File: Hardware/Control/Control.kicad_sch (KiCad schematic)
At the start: 44 parts, among them SW1 EN11-HSM1AF20, SW2 KO128B2007, SW3 Conn_01x04, U1 XRA1402IG16TR-F, U2 FT230XS-U, U4 ATMEGA328P-AU, U5 ESDALD05UD4, Y1 ABM8AIG-20.000MHZ-4-T

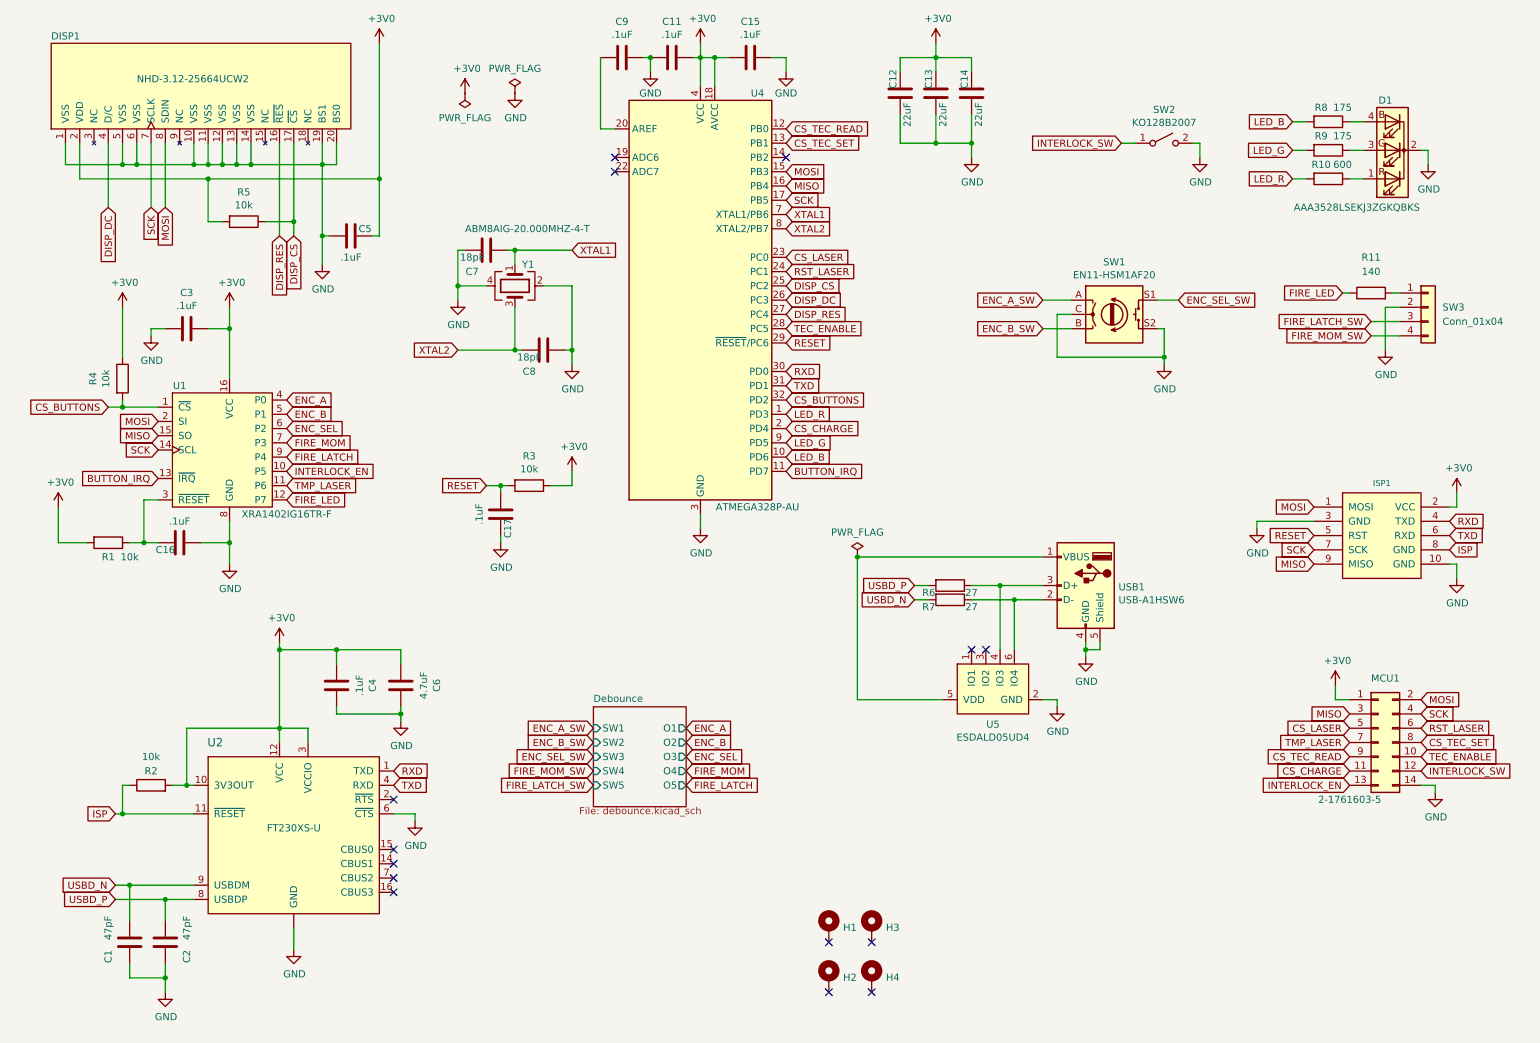
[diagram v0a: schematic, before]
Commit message: Move to AVR128DB64 MCU
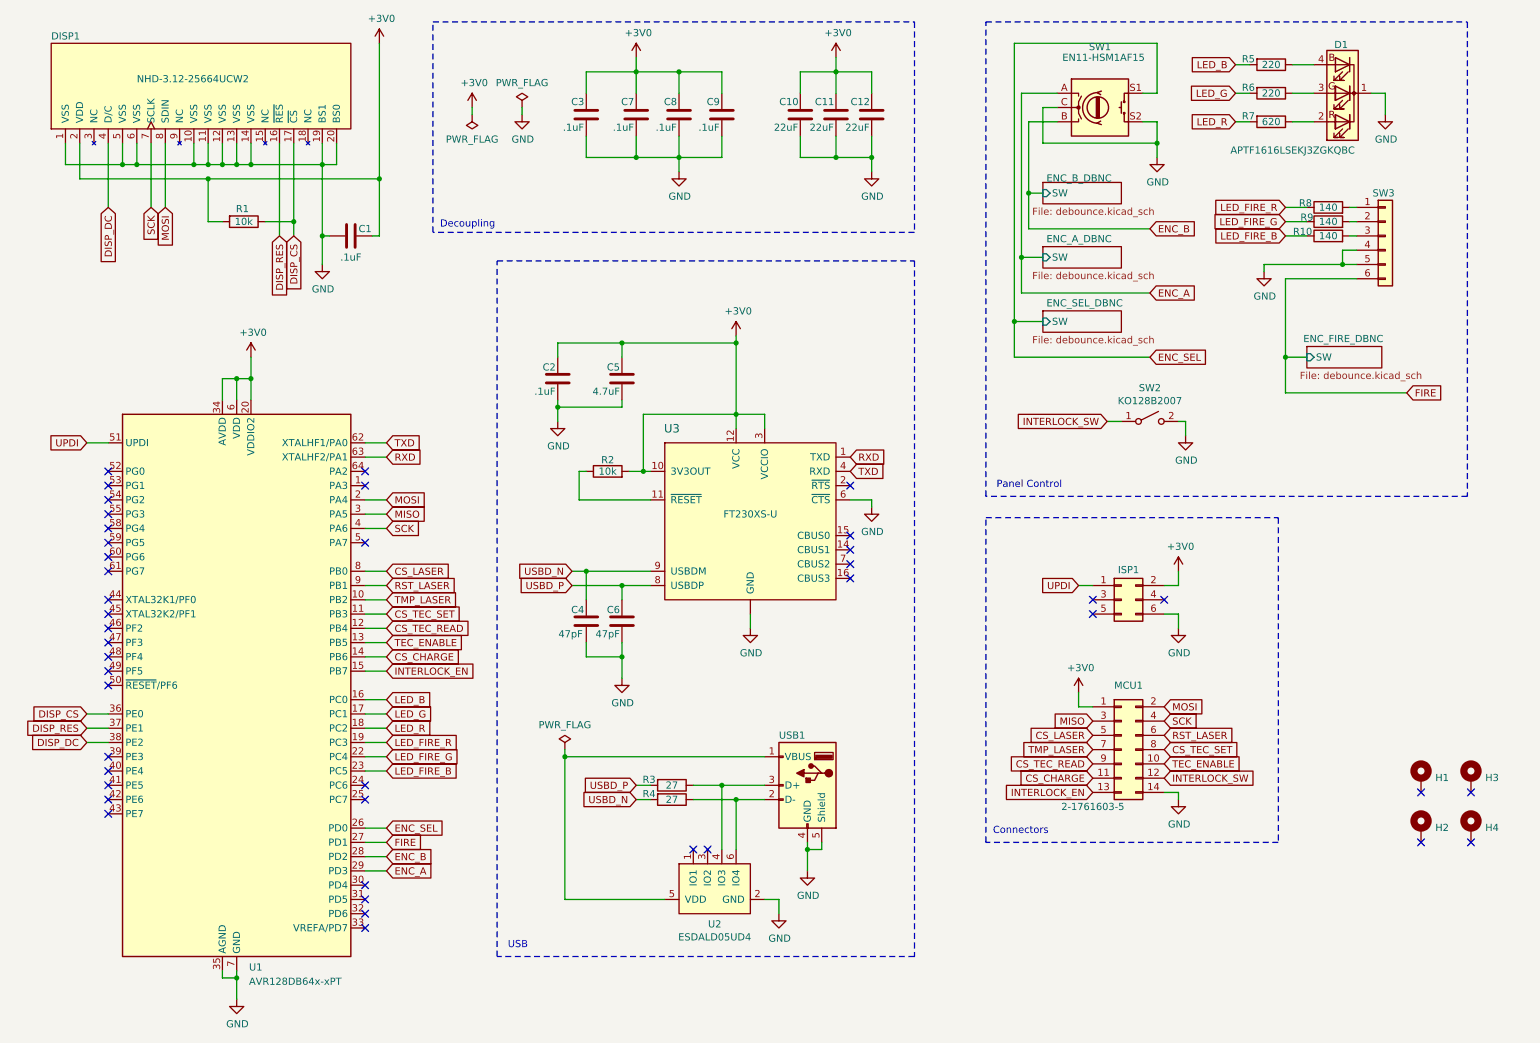
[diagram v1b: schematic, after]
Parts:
- removed C11, C15, C16, C17: .1uF, Capacitor_SMD:C_0805_2012Metric, symbol Device:C
- removed D1: AAA3528LSEKJ3ZGKQBKS, LED_SMD:LED_Avago_PLCC4_3.2x2.8mm_CW, symbol Device:LED_RKGB
- removed ISP1: AVR_ISP_10_SERIAL, pepin-footprints:TC2050-IDC, symbol pepin_con:AVR_ISP_10_SERIAL
- removed R1, R3, R4: 10k, Resistor_SMD:R_0805_2012Metric, symbol Device:R
- removed SW3: Conn_01x04, Connector_PinHeader_2.54mm:PinHeader_1x04_P2.54mm_Vertical, symbol Connector_Generic:Conn_01x04
- removed U1: XRA1402IG16TR-F, Package_SO:TSSOP-16_4.4x5mm_P0.65mm, symbol Components:XRA1402IG16TR-F
- removed U4: ATMEGA328P-AU, Package_QFP:TQFP-32_7x7mm_P0.8mm, symbol MCU_Microchip_ATmega:ATmega328P-A
- removed Y1: ABM8AIG-20.000MHZ-4-T, Crystal:Crystal_SMD_3225-4Pin_3.2x2.5mm, symbol Device:Crystal_GND24
- added D1: APTF1616LSEKJ3ZGKQBC, Components:LED_Kingbright_KRGB_1.6x1.6mm, symbol Device:LED_KRGB
- added ISP1: 61200621621, Connector_IDC:IDC-Header_2x03_P2.54mm_Vertical, symbol Connector_Generic:Conn_02x03_Odd_Even
- added R10, R9: 140, Resistor_SMD:R_0805_2012Metric, symbol Device:R
- added SW3: Conn_01x06, Connector_PinHeader_2.54mm:PinHeader_1x06_P2.54mm_Vertical, symbol Connector_Generic:Conn_01x06
- added U1: AVR128DB64x-xPT, Package_QFP:TQFP-64_10x10mm_P0.5mm, symbol MCU_Microchip_AVR_Dx:AVR128DB64x-xPT
- C1: renamed from C5; Product Number (none) -> CGA4J2X8R1H104K125AE
- C10: renamed from C12; Product Number CL31A226KAHNNNE -> LMJ316BB7226KLHT
- C11: renamed from C13; Product Number CL31A226KAHNNNE -> LMJ316BB7226KLHT
- C12: renamed from C14; Product Number CL31A226KAHNNNE -> LMJ316BB7226KLHT
- C2: renamed from C4; Product Number (none) -> CGA4J2X8R1H104K125AE
- C3, C9: Product Number (none) -> CGA4J2X8R1H104K125AE
- C4: renamed from C1; Product Number (none) -> C0805C470J1GAC
- C5: renamed from C6; Product Number (none) -> C0805C475K4RACAUTO
- C6: renamed from C2; Product Number (none) -> C0805C470J1GAC
- C7, C8: value 18pF -> .1uF; Product Number C0805C180J5HACTU -> CGA4J2X8R1H104K125AE
- R1: renamed from R5; Product Number (none) -> ERA-6AEB103V
- R2: Product Number (none) -> ERA-6AEB103V
- R3: renamed from R6; Product Number (none) -> CR0805-FX-27R0ELF
- R4: renamed from R7; Product Number (none) -> CR0805-FX-27R0ELF
- R5: renamed from R8; value 175 -> 220; Product Number (none) -> ERA-6AEB221V
- R6: renamed from R9; value 175 -> 220; Product Number (none) -> ERA-6AEB221V
- R7: renamed from R10; value 600 -> 620; Product Number (none) -> CR0805-FX-6200ELF
- R8: renamed from R11; Product Number (none) -> CRCW0805140RFKEA
- SW1: value EN11-HSM1AF20 -> EN11-HSM1AF15; Product Number EN11-HSM1AF20 -> EN11-HSM1AF15
- USB1: value USB-A1HSW6 -> UJ2-A-HR-G-TH; Product Number USB-A1HSW6 -> UJ2-A-HR-G-TH
- renumbered U5 to U2, U2 to U3
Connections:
- net ENC_A_SW is gone; now on net ENC_A: SW1.A
- net ENC_B_SW is gone; now on net ENC_B: SW1.B
- net ENC_SEL_SW is gone; now on net ENC_SEL: SW1.S1
- net XTAL1 is gone; now on net GND: C7.1
- net XTAL2 is gone; now on net +3V0: C8.2
- net +3V0: now also C7.2, C9.2, ISP1.2 (Pin_2), U1.20 (VDDIO2), U1.34 (AVDD), U1.56 (VDD), U1.6 (VDD)
- net CS_CHARGE: now also U1.14 (PB6)
- net CS_LASER: now also U1.8 (PB0)
- net CS_TEC_READ: now also U1.12 (PB4)
- net CS_TEC_SET: now also U1.11 (PB3)
- net DISP_CS: now also U1.36 (PE0)
- net DISP_DC: now also U1.38 (PE2)
- net DISP_RES: now also U1.37 (PE1)
- net ENC_A: now also U1.29 (PD3)
- net ENC_B: now also U1.28 (PD2)
- net ENC_SEL: now also U1.26 (PD0)
- net GND: now also C9.1, D1.1 (K), ISP1.6 (Pin_6), SW3.4 (Pin_4), SW3.5 (Pin_5), U1.21 (GND), U1.35 (AGND), U1.57 (GND), U1.7 (GND); no longer C7.2, C9.2
- net INTERLOCK_EN: now also U1.15 (PB7)
- net LED_B: now also U1.16 (PC0)
- net LED_G: now also U1.17 (PC1)
- net LED_R: now also U1.18 (PC2)
- net MISO: now also U1.3 (PA5)
- net MOSI: now also U1.2 (PA4)
- net RST_LASER: now also U1.9 (PB1)
- net RXD: now also U1.63 (XTALHF2/PA1)
- net SCK: now also U1.4 (PA6)
- net TEC_ENABLE: now also U1.13 (PB5)
- net TMP_LASER: now also U1.10 (PB2)
- net TXD: now also U1.62 (XTALHF1/PA0)
- net at R5.1: now also D1.4 (BA)
- net at R6.1: now also D1.3 (GA)
- net at R7.1: now also D1.2 (RA)
- net at R8.2: now also SW3.1 (Pin_1)
- net FIRE_LED renamed LED_FIRE_R
- net LED_FIRE_R: now also U1.19 (PC3)
- net ISP: no longer names the net of R2.1, U3.11 (~{RESET})
- new net: R9.2, SW3.2 (Pin_2)
- new net: R10.2, SW3.3 (Pin_3)
- new net FIRE: SW3.6 (Pin_6), U1.27 (PD1)
- new net LED_FIRE_B: R10.1, U1.23 (PC5)
- new net LED_FIRE_G: R9.1, U1.22 (PC4)
- new net UPDI: ISP1.1 (Pin_1), U1.51 (UPDI)
- no-connect marks 14 -> 43
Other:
- removed sheet Debounce
- added sheet ENC_A_DBNC (debounce.kicad_sch)
- added sheet ENC_B_DBNC (debounce.kicad_sch)
- added sheet ENC_FIRE_DBNC (debounce.kicad_sch)
- added sheet ENC_SEL_DBNC (debounce.kicad_sch)
- note added: "Connectors"
- note added: "Decoupling"
- note added: "Panel Control"
- note added: "USB"
- moved on the sheet: C10, C11, C12, C2, C4, C5, C6, H1, H2, H3, H4, MCU1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

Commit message: Minor hardware fix for control board; requires software changes too
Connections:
- net CS_CHARGE: now also U1.13 (PB5); no longer U1.14 (PB6)
- net CS_LASER: now also U1.9 (PB1); no longer U1.8 (PB0)
- net CS_TEC_READ: now also U1.11 (PB3); no longer U1.12 (PB4)
- net CS_TEC_SET: now also U1.10 (PB2); no longer U1.11 (PB3)
- net INTERLOCK_EN: now also U1.31 (PD5); no longer U1.15 (PB7)
- net RST_LASER: now also U1.8 (PB0); no longer U1.9 (PB1)
- net TEC_ENABLE: now also U1.12 (PB4); no longer U1.13 (PB5)
- net TMP_LASER: now also U1.30 (PD4); no longer U1.10 (PB2)
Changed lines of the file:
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@@
 	(title_block
 		(title "Laser Control Board")
-		(date "2024-03-30")
-		(rev "2.0")
+		(date "2024-12-01")
+		(rev "2.1")
 		(company "Brian Pepin")
 	)
@@
 	)
 	(no_connect
-		(at 76.2 171.45)
+		(at 76.2 130.81)
 	)
 	(no_connect
@@
 	)
 	(no_connect
-		(at 76.2 168.91)
+		(at 76.2 128.27)
 	)
 	(no_connect
@@
 	(wire
 		(pts
-			(xy 76.2 118.11) (xy 80.01 118.11)
+			(xy 76.2 168.91) (xy 80.01 168.91)
 		)
 		(stroke
@@
 	(wire
 		(pts
-			(xy 76.2 130.81) (xy 80.01 130.81)
+			(xy 76.2 171.45) (xy 80.01 171.45)
 		)
 		(stroke
@@
 	(wire
 		(pts
-			(xy 76.2 128.27) (xy 80.01 128.27)
+			(xy 76.2 118.11) (xy 80.01 118.11)
 		)
 		(stroke
@@
 	(global_label "TMP_LASER"
 		(shape input)
-		(at 80.01 118.11 0)
+		(at 80.01 168.91 0)
 		(fields_autoplaced yes)
 		(effects
@@
 		)
 		(property "Intersheetrefs" "${INTERSHEET_REFS}"
-			(at 92.7428 118.11 0)
+			(at 92.7428 168.91 0)
 			(effects
 				(font
@@
 	(global_label "INTERLOCK_EN"
 		(shape input)
-		(at 80.01 130.81 0)
+		(at 80.01 171.45 0)
 		(fields_autoplaced yes)
 		(effects
@@
 		)
 		(property "Intersheetrefs" "${INTERSHEET_REFS}"
-			(at 96.0086 130.81 0)
+			(at 96.0086 171.45 0)
 			(effects
 				(font
@@
 	(global_label "RST_LASER"
 		(shape input)
-		(at 80.01 115.57 0)
+		(at 80.01 113.03 0)
 		(fields_autoplaced yes)
 		(effects
@@
 		)
 		(property "Intersheetrefs" "${INTERSHEET_REFS}"
-			(at 92.5009 115.57 0)
+			(at 92.5009 113.03 0)
 			(effects
 				(font
@@
 	(global_label "CS_TEC_SET"
 		(shape input)
-		(at 80.01 120.65 0)
+		(at 80.01 118.11 0)
 		(fields_autoplaced yes)
 		(effects
@@
 		)
 		(property "Intersheetrefs" "${INTERSHEET_REFS}"
-			(at 93.4684 120.65 0)
+			(at 93.4684 118.11 0)
 			(effects
 				(font
@@
 	(global_label "CS_CHARGE"
 		(shape input)
-		(at 80.01 128.27 0)
+		(at 80.01 125.73 0)
 		(fields_autoplaced yes)
 		(effects
@@
 		)
 		(property "Intersheetrefs" "${INTERSHEET_REFS}"
-			(at 93.1662 128.27 0)
+			(at 93.1662 125.73 0)
 			(effects
 				(font
@@
 	(global_label "CS_LASER"
 		(shape input)
-		(at 80.01 113.03 0)
+		(at 80.01 115.57 0)
 		(fields_autoplaced yes)
 		(effects
@@
 		)
 		(property "Intersheetrefs" "${INTERSHEET_REFS}"
-			(at 91.5333 113.03 0)
+			(at 91.5333 115.57 0)
 			(effects
 				(font
@@
 	(global_label "CS_TEC_READ"
 		(shape input)
-		(at 80.01 123.19 0)
+		(at 80.01 120.65 0)
 		(fields_autoplaced yes)
 		(effects
@@
 		)
 		(property "Intersheetrefs" "${INTERSHEET_REFS}"
-			(at 94.9199 123.19 0)
+			(at 94.9199 120.65 0)
 			(effects
 				(font
@@
 	(global_label "TEC_ENABLE"
 		(shape input)
-		(at 80.01 125.73 0)
+		(at 80.01 123.19 0)
 		(fields_autoplaced yes)
 		(effects
@@
 		)
 		(property "Intersheetrefs" "${INTERSHEET_REFS}"
-			(at 93.7104 125.73 0)
+			(at 93.7104 123.19 0)
 			(effects
 				(font
@@
 			)
 		)
-		(property "Datasheet" " ~"
+		(property "Datasheet" "~"
 			(at 151.13 152.4 0)
 			(effects
@@
 			)
 		)
-		(property "Description" ""
+		(property "Description" "USB Type A connector"
 			(at 154.94 151.13 0)
 			(effects

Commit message: Fix bad footprint for RGG LED
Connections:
- net LED_B: now also U1.18 (PC2); no longer U1.16 (PC0)
- net LED_R: now also U1.16 (PC0); no longer U1.18 (PC2)
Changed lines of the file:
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@@
 	(global_label "LED_R"
 		(shape input)
+		(at 80.01 135.89 0)
+		(fields_autoplaced yes)
+		(effects
+			(font
+				(size 1.27 1.27)
+			)
+			(justify left)
+		)
+		(property "Intersheetrefs" "${INTERSHEET_REFS}"
+			(at 88.0257 135.89 0)
+			(effects
+				(font
+					(size 1.27 1.27)
+				)
+				(justify left)
+				(hide yes)
+			)
+		)
+	)
+	(global_label "INTERLOCK_SW"
+		(shape input)
+		(at 208.28 86.36 180)
+		(fields_autoplaced yes)
+		(effects
+			(font
+				(size 1.27 1.27)
+			)
+			(justify right)
+		)
+		(property "Intersheetrefs" "${INTERSHEET_REFS}"
+			(at 192.1 86.36 0)
+			(effects
+				(font
+					(size 1.27 1.27)
+				)
+				(justify right)
+				(hide yes)
+			)
+		)
+	)
+	(global_label "ENC_A"
+		(shape input)
+		(at 80.01 166.37 0)
+		(fields_autoplaced yes)
+		(effects
+			(font
+				(size 1.27 1.27)
+			)
+			(justify left)
+		)
+		(property "Intersheetrefs" "${INTERSHEET_REFS}"
+			(at 88.1399 166.2906 0)
+			(effects
+				(font
+					(size 1.27 1.27)
+				)
+				(justify left)
+				(hide yes)
+			)
+		)
+	)
+	(global_label "LED_FIRE_G"
+		(shape input)
+		(at 240.03 50.8 180)
+		(fields_autoplaced yes)
+		(effects
+			(font
+				(size 1.27 1.27)
+			)
+			(justify right)
+		)
+		(property "Intersheetrefs" "${INTERSHEET_REFS}"
+			(at 226.9343 50.8 0)
+			(effects
+				(font
+					(size 1.27 1.27)
+				)
+				(justify right)
+				(hide yes)
+			)
+		)
+	)
+	(global_label "RXD"
+		(shape input)
+		(at 80.01 92.71 0)
+		(fields_autoplaced yes)
+		(effects
+			(font
+				(size 1.27 1.27)
+			)
+			(justify left)
+		)
+		(property "Intersheetrefs" "${INTERSHEET_REFS}"
+			(at 86.0905 92.71 0)
+			(effects
+				(font
+					(size 1.27 1.27)
+				)
+				(justify left)
+				(hide yes)
+			)
+		)
+	)
+	(global_label "DISP_CS"
+		(shape input)
+		(at 26.67 138.43 180)
+		(fields_autoplaced yes)
+		(effects
+			(font
+				(size 1.27 1.27)
+			)
+			(justify right)
+		)
+		(property "Intersheetrefs" "${INTERSHEET_REFS}"
+			(at 16.5376 138.43 0)
+			(effects
+				(font
+					(size 1.27 1.27)
+				)
+				(justify right)
+				(hide yes)
+			)
+		)
+	)
+	(global_label "RXD"
+		(shape input)
+		(at 162.56 92.71 0)
+		(fields_autoplaced yes)
+		(effects
+			(font
+				(size 1.27 1.27)
+			)
+			(justify left)
+		)
+		(property "Intersheetrefs" "${INTERSHEET_REFS}"
+			(at 168.6405 92.71 0)
+			(effects
+				(font
+					(size 1.27 1.27)
+				)
+				(justify left)
+				(hide yes)
+			)
+		)
+	)
+	(global_label "CS_LASER"
+		(shape input)
+		(at 80.01 115.57 0)
+		(fields_autoplaced yes)
+		(effects
+			(font
+				(size 1.27 1.27)
+			)
+			(justify left)
+		)
+		(property "Intersheetrefs" "${INTERSHEET_REFS}"
+			(at 91.5333 115.57 0)
+			(effects
+				(font
+					(size 1.27 1.27)
+				)
+				(justify left)
+				(hide yes)
+			)
+		)
+	)
+	(global_label "DISP_RES"
+		(shape input)
+		(at 60.96 53.34 270)
+		(fields_autoplaced yes)
+		(effects
+			(font
+				(size 1.27 1.27)
+			)
+			(justify right)
+		)
+		(property "Intersheetrefs" "${INTERSHEET_REFS}"
+			(at 60.96 64.6214 90)
+			(effects
+				(font
+					(size 1.27 1.27)
+				)
+				(justify right)
+				(hide yes)
+			)
+		)
+	)
+	(global_label "LED_B"
+		(shape input)
 		(at 80.01 140.97 0)
 		(fields_autoplaced yes)
@@
 			(effects
 				(font
-					(size 1.27 1.27)
-				)
-				(justify left)
-				(hide yes)
-			)
-		)
-	)
-	(global_label "INTERLOCK_SW"
-		(shape input)
-		(at 208.28 86.36 180)
-		(fields_autoplaced yes)
-		(effects
-			(font
-				(size 1.27 1.27)
-			)
-			(justify right)
-		)
-		(property "Intersheetrefs" "${INTERSHEET_REFS}"
-			(at 192.1 86.36 0)
-			(effects
-				(font
-					(size 1.27 1.27)
-				)
-				(justify right)
-				(hide yes)
-			)
-		)
-	)
-	(global_label "ENC_A"
-		(shape input)
-		(at 80.01 166.37 0)
-		(fields_autoplaced yes)
-		(effects
-			(font
-				(size 1.27 1.27)
-			)
-			(justify left)
-		)
-		(property "Intersheetrefs" "${INTERSHEET_REFS}"
-			(at 88.1399 166.2906 0)
-			(effects
-				(font
-					(size 1.27 1.27)
-				)
-				(justify left)
-				(hide yes)
-			)
-		)
-	)
-	(global_label "LED_FIRE_G"
-		(shape input)
-		(at 240.03 50.8 180)
-		(fields_autoplaced yes)
-		(effects
-			(font
-				(size 1.27 1.27)
-			)
-			(justify right)
-		)
-		(property "Intersheetrefs" "${INTERSHEET_REFS}"
-			(at 226.9343 50.8 0)
-			(effects
-				(font
-					(size 1.27 1.27)
-				)
-				(justify right)
-				(hide yes)
-			)
-		)
-	)
-	(global_label "RXD"
-		(shape input)
-		(at 80.01 92.71 0)
-		(fields_autoplaced yes)
-		(effects
-			(font
-				(size 1.27 1.27)
-			)
-			(justify left)
-		)
-		(property "Intersheetrefs" "${INTERSHEET_REFS}"
-			(at 86.0905 92.71 0)
-			(effects
-				(font
-					(size 1.27 1.27)
-				)
-				(justify left)
-				(hide yes)
-			)
-		)
-	)
-	(global_label "DISP_CS"
-		(shape input)
-		(at 26.67 138.43 180)
-		(fields_autoplaced yes)
-		(effects
-			(font
-				(size 1.27 1.27)
-			)
-			(justify right)
-		)
-		(property "Intersheetrefs" "${INTERSHEET_REFS}"
-			(at 16.5376 138.43 0)
-			(effects
-				(font
-					(size 1.27 1.27)
-				)
-				(justify right)
-				(hide yes)
-			)
-		)
-	)
-	(global_label "RXD"
-		(shape input)
-		(at 162.56 92.71 0)
-		(fields_autoplaced yes)
-		(effects
-			(font
-				(size 1.27 1.27)
-			)
-			(justify left)
-		)
-		(property "Intersheetrefs" "${INTERSHEET_REFS}"
-			(at 168.6405 92.71 0)
-			(effects
-				(font
-					(size 1.27 1.27)
-				)
-				(justify left)
-				(hide yes)
-			)
-		)
-	)
-	(global_label "CS_LASER"
-		(shape input)
-		(at 80.01 115.57 0)
-		(fields_autoplaced yes)
-		(effects
-			(font
-				(size 1.27 1.27)
-			)
-			(justify left)
-		)
-		(property "Intersheetrefs" "${INTERSHEET_REFS}"
-			(at 91.5333 115.57 0)
-			(effects
-				(font
-					(size 1.27 1.27)
-				)
-				(justify left)
-				(hide yes)
-			)
-		)
-	)
-	(global_label "DISP_RES"
-		(shape input)
-		(at 60.96 53.34 270)
-		(fields_autoplaced yes)
-		(effects
-			(font
-				(size 1.27 1.27)
-			)
-			(justify right)
-		)
-		(property "Intersheetrefs" "${INTERSHEET_REFS}"
-			(at 60.96 64.6214 90)
-			(effects
-				(font
-					(size 1.27 1.27)
-				)
-				(justify right)
-				(hide yes)
-			)
-		)
-	)
-	(global_label "LED_B"
-		(shape input)
-		(at 80.01 135.89 0)
-		(fields_autoplaced yes)
-		(effects
-			(font
-				(size 1.27 1.27)
-			)
-			(justify left)
-		)
-		(property "Intersheetrefs" "${INTERSHEET_REFS}"
-			(at 88.0257 135.89 0)
-			(effects
-				(font

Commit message: Minor tweaks
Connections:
- net VBUS: now reaches U2.5 (VDD), USB1.1 (VBUS)
- net D-: now reaches R4.1, U2.6 (IO4), USB1.2 (D-)
- net D+: now reaches R3.1, U2.4 (IO3), USB1.3 (D+)
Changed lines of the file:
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@@
+		)
+	)
+	(label "VBUS"
+		(at 142.24 146.05 0)
+		(effects
+			(font
+				(size 1.27 1.27)
+			)
+			(justify left bottom)
+		)
+	)
+	(label "D-"
+		(at 142.24 153.67 0)
+		(effects
+			(font
+				(size 1.27 1.27)
+			)
+			(justify left bottom)
+		)
+	)
+	(label "D+"
+		(at 142.24 151.13 0)
+		(effects
+			(font
+				(size 1.27 1.27)
+			)
+			(justify left bottom)
 		)
 	)
